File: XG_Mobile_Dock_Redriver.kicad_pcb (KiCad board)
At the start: 4 copper layers, 220 x 65 mm, 153 parts, among them J1 5-1775443-8, J10 SWD, J11 UART, J12 I2C1, J13 39301240, J14 SWD, J15 SWD, J17 8730, J2 20455-040E-76, J20 SWD, J21 SWD, J22 SWD, J23 SWD, J24 SWD, J25 SWD, J26 SWD, J27 SWD, J28 SWD, J29 SWD, J3 20455-040E-76, J30 SWD, J31 SWD, J32 SWD, J33 SWD, J4 3-2362375-4, J5 USB_C_Receptacle, J6 455860005, Q16 AO3401A, Q17 2N7002W, SW1 SW_Push, U1 DS320PR810NJXR, U12 STM32F030C8Tx, U2 DS320PR810NJXR

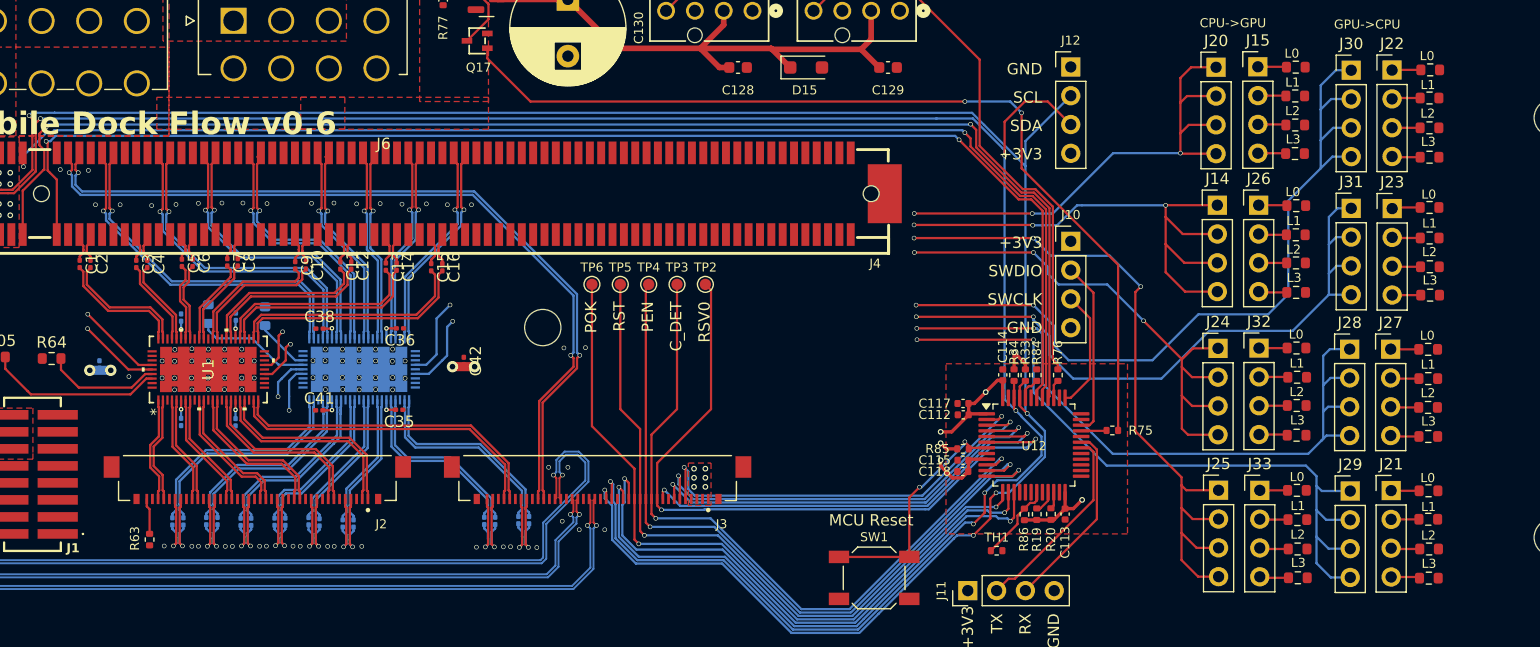
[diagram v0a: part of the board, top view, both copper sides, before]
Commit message: fixed traces for pcie with filet
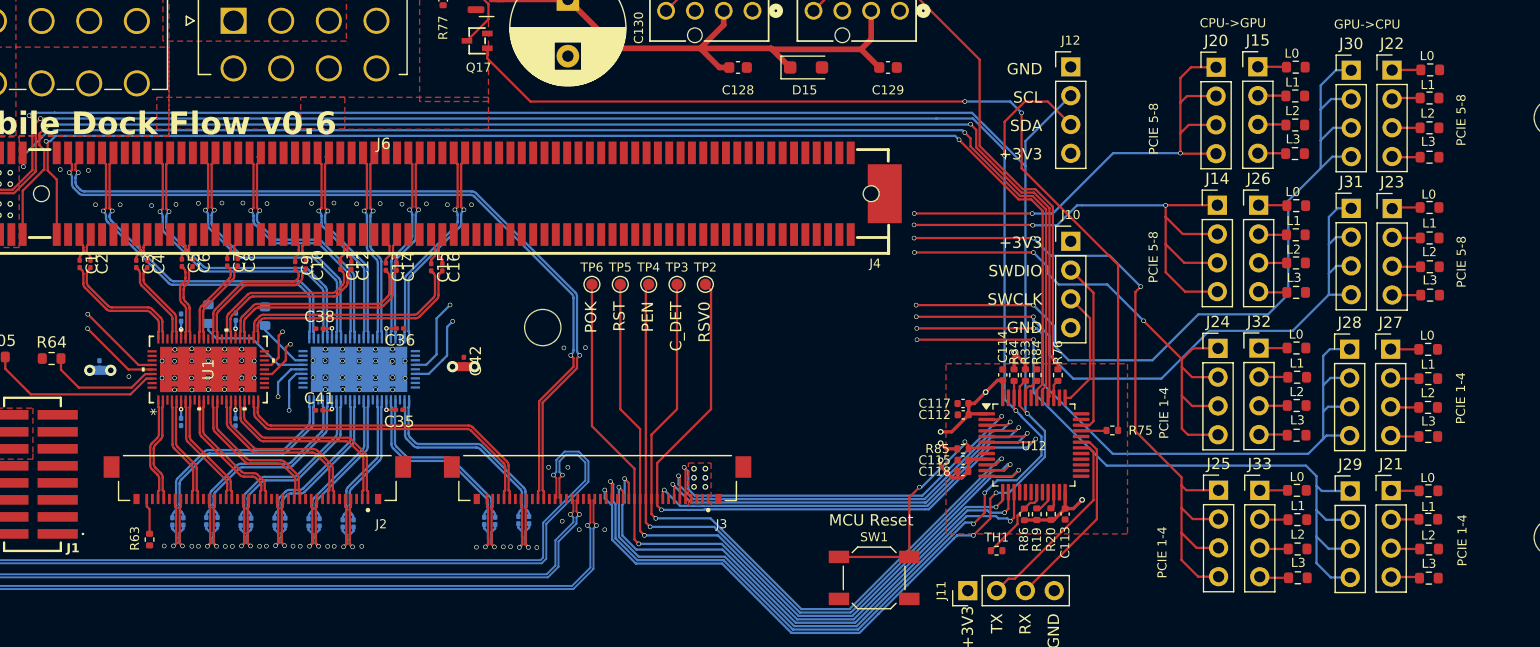
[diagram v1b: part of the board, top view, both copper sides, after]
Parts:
- moved C25 0.10 mm to (113.1, 89.1)
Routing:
- net GND: track 6.51 -> 51.1 mm
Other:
- board text added: "PCIE 1-4"
- board text added: "PCIE 5-8"

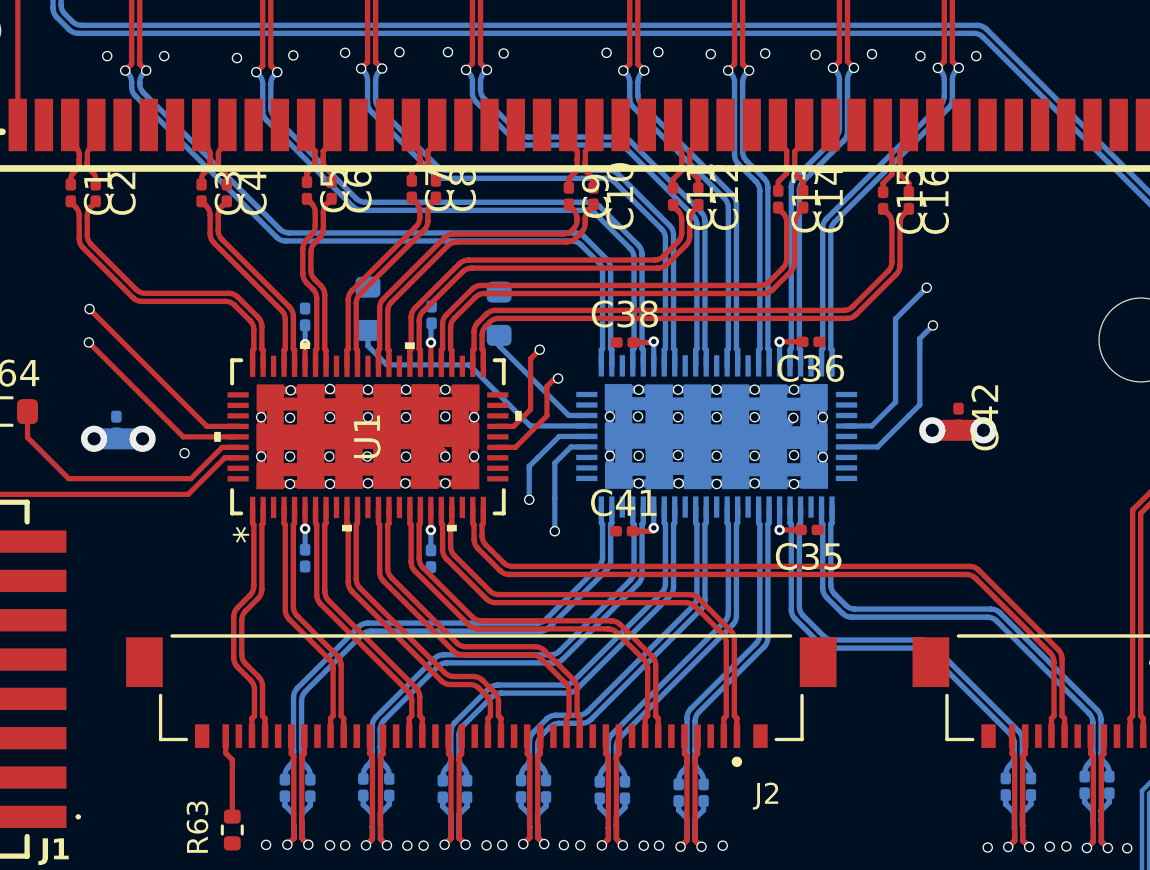
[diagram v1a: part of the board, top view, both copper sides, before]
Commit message: added more vias and fixed some issues with traces
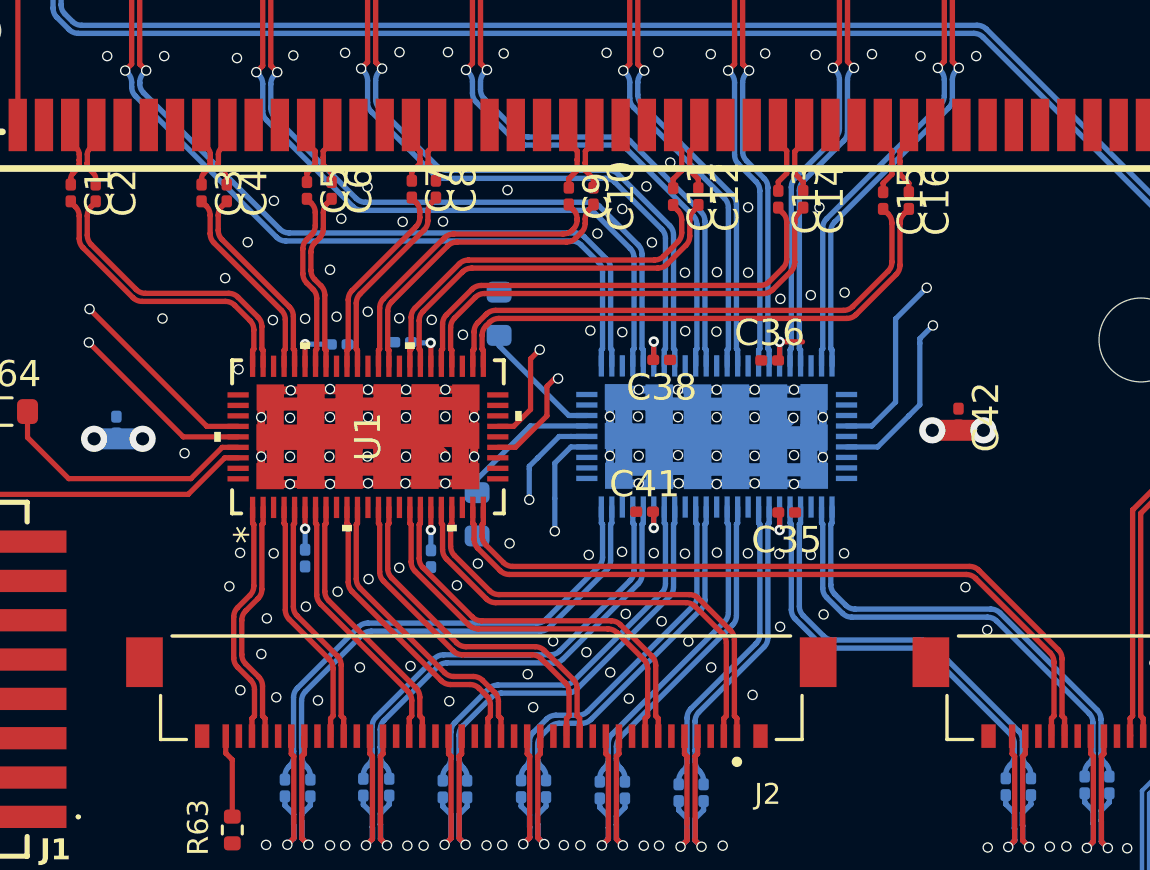
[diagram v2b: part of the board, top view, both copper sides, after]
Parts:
- moved R65 8.88 mm to (108.5, 78.6), turned to 90 degrees
- moved C36 1.73 mm to (119.6, 72.7), turned to 0 degrees
- moved C33 1.67 mm to (103.2, 72.1), turned to 180 degrees
- moved C38 1.55 mm to (115.5, 72.7), turned to 180 degrees
- moved C39 1.52 mm to (105.6, 72.0), turned to 0 degrees
- moved C35 1.09 mm to (120.3, 78.5)
- moved C41 1.07 mm to (114.8, 78.5)
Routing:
- net Net-(J30-Pin_1): track 139.5 -> 128.9 mm
- net Net-(J31-Pin_1): track 127.6 -> 118.0 mm
- net Net-(U2-MODE): track 10.2 -> 5.54 mm
- net +3V3: track 271.3 -> 273.4 mm
- net Net-(J24-Pin_1): track 112.6 -> 114.5 mm
- net Net-(J25-Pin_1): track 127.4 -> 129.0 mm
- net GND: vias 100 -> 177

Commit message: more tweaks and fixes
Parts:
- removed R105, R106: 24.9k, Resistor_SMD:R_0603_1608Metric
- moved C40 1.86 mm to (106.4, 78.4), turned to 0 degrees
- moved C34 1.84 mm to (102.2, 78.4), turned to 180 degrees
- moved J17 0.26 mm to (75.6, 78.4)
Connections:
- U1 pad 62: Net-(U1-RX_DET/SCL) -> unconnected-(U1-RX_DET/SCL-Pad62)
- U2 pad 62: Net-(U2-RX_DET/SCL) -> unconnected-(U2-RX_DET/SCL-Pad62)
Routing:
- net Net-(U1-RX_DET/SCL): track 15.5 -> 0.00 mm
- net Net-(J30-Pin_1): track 128.9 -> 140.1 mm
- net Net-(J31-Pin_1): track 118.0 -> 127.5 mm
- net Net-(U2-RX_DET/SCL): track 4.85 -> 0.00 mm
- net Net-(J25-Pin_1): track 129.0 -> 129.8 mm
- net Net-(J24-Pin_1): track 114.5 -> 115.0 mm
